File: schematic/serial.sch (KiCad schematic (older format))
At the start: 8 parts, among them J4 CONN_01X09, J5 DB9_MALE, U401 MAX232

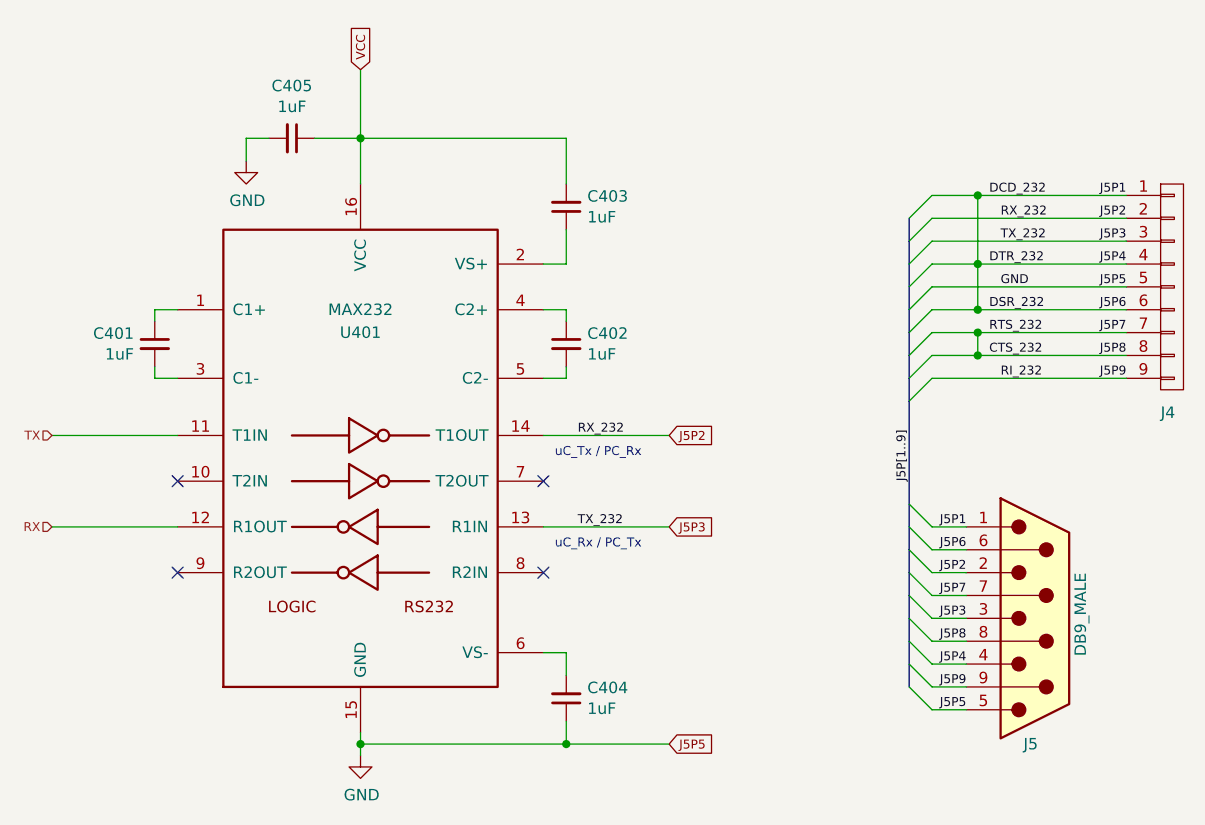
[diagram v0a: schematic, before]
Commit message: [L3] Update schematic with new NVRAM signals
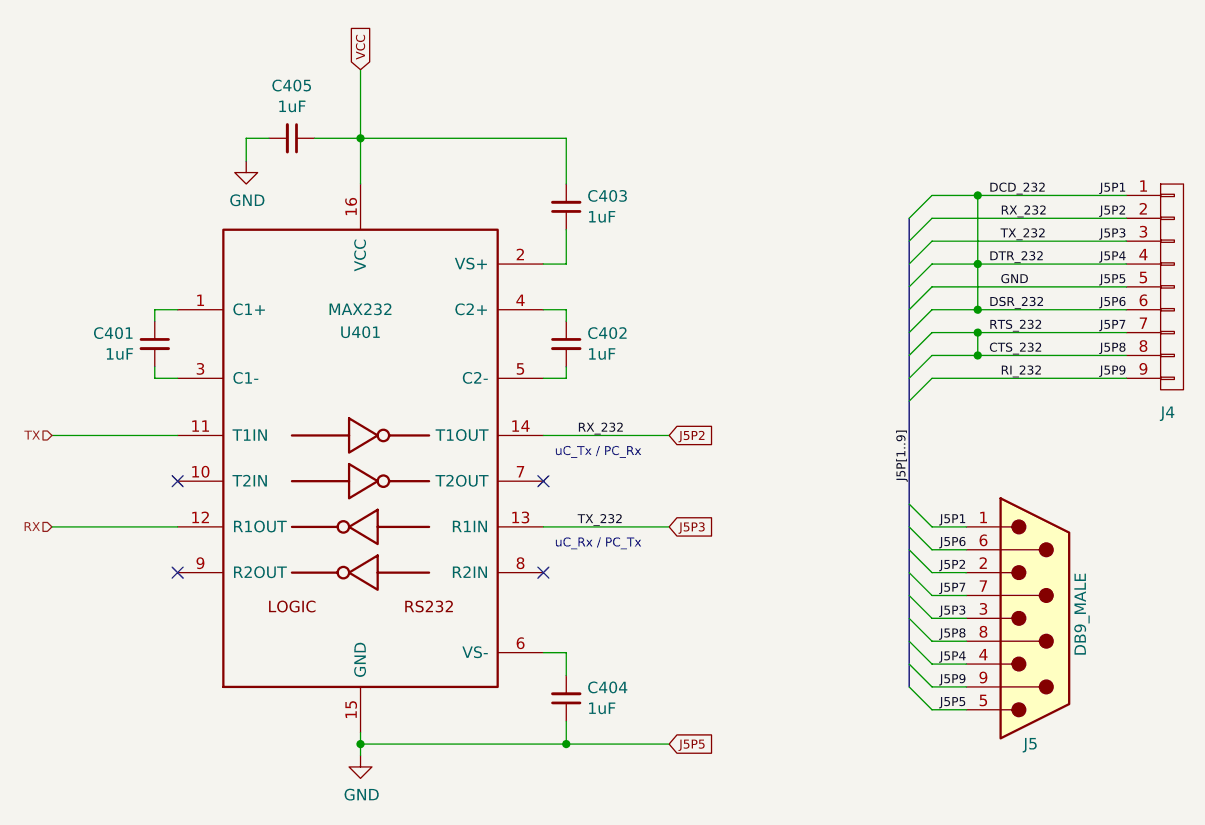
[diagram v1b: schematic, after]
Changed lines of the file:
@@
 EELAYER 26 0
 EELAYER END
-$Descr A4 11693 8268
+$Descr USLetter 11000 8500
 encoding utf-8
 Sheet 4 4
@@
 $EndComp
 Wire Wire Line
-	5350 2150 5550 2150
-Wire Wire Line
-	5550 2150 6200 2150
+	5350 2150 6200 2150
 Wire Wire Line
 	6200 2250 5350 2250
 Wire Wire Line
-	5350 2450 5550 2450
-Wire Wire Line
-	5550 2450 6200 2450
+	5350 2450 6200 2450
 Wire Wire Line
 	6200 2550 5350 2550
 Wire Wire Line
-	5350 2650 5550 2650
-Wire Wire Line
-	5550 2650 6200 2650
-Wire Wire Line
-	5350 2750 5550 2750
-Wire Wire Line
-	5550 2750 6200 2750
+	5350 2650 6200 2650
+Wire Wire Line
+	5350 2750 6200 2750
 Wire Wire Line
 	6200 2950 5350 2950
@@
 	5350 3600 5250 3500
 Wire Bus Line
-	5250 2250 5250 2350
-Wire Bus Line
-	5250 2350 5250 2450
-Wire Bus Line
-	5250 2450 5250 2550
-Wire Bus Line
-	5250 2550 5250 2650
-Wire Bus Line
-	5250 2650 5250 2750
-Wire Bus Line
-	5250 2750 5250 2850
-Wire Bus Line
-	5250 2850 5250 2950
-Wire Bus Line
-	5250 2950 5250 3050
-Wire Bus Line
-	5250 3050 5250 3500
-Wire Bus Line
-	5250 3500 5250 3600
-Wire Bus Line
-	5250 3600 5250 3700
-Wire Bus Line
-	5250 3700 5250 3800
-Wire Bus Line
-	5250 3800 5250 3900
-Wire Bus Line
-	5250 3900 5250 4000
-Wire Bus Line
-	5250 4000 5250 4100
-Wire Bus Line
-	5250 4100 5250 4200
-Wire Bus Line
-	5250 4200 5250 4300
+	5250 2250 5250 4300
 Text Label 5250 3400 1    39   ~ 0
 J5P[1..9]
@@
 	3750 1900 3750 2100
 Wire Wire Line
-	2650 1900 2850 1900
-Wire Wire Line
-	2850 1900 3750 1900
-Wire Wire Line
-	2850 1600 2850 1900
-Wire Wire Line
-	2850 1900 2850 2100
+	2650 1900 3750 1900
+Wire Wire Line
+	2850 1600 2850 2100
 Connection ~ 2850 1900
 Wire Wire Line
@@
 	2350 1900 2450 1900
 Wire Wire Line
-	2850 4500 2850 4550
-Wire Wire Line
-	2850 4550 2850 4600
-Wire Wire Line
-	2850 4550 3750 4550
-Wire Wire Line
-	3750 4550 4200 4550
+	2850 4500 2850 4600
+Wire Wire Line
+	2850 4550 4200 4550
 Wire Wire Line
 	3750 4550 3750 4450
@@
 RI_232
 Wire Wire Line
-	5350 2850 5550 2850
-Wire Wire Line
-	5550 2850 6200 2850
+	5350 2850 6200 2850
 Connection ~ 5550 2850
 Wire Wire Line
-	5550 2150 5550 2450
-Wire Wire Line
-	5550 2450 5550 2650
+	5550 2150 5550 2650
 Connection ~ 5550 2150
 Connection ~ 5550 2450
